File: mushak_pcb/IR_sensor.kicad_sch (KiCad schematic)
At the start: 24 parts, among them J6 IR_1, J7 IR_1, J8 IR_1, J9 IR_1, Q2 DMN3065LW-7, Q3 DMN3065LW-7, Q4 DMN3065LW-7, Q5 DMN3065LW-7

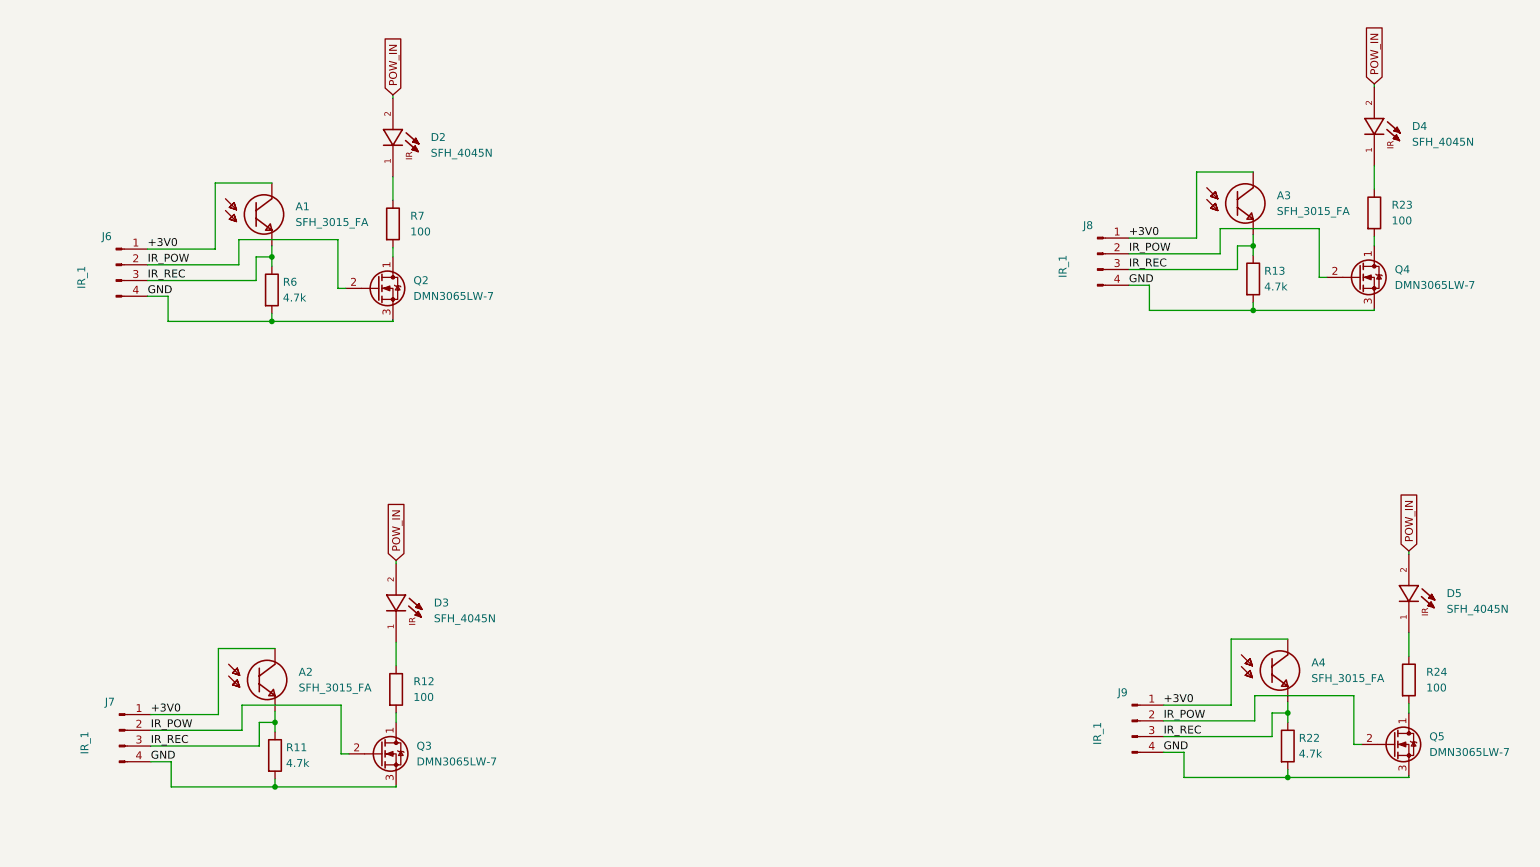
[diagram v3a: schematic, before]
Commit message: made draft pcb footprint placement
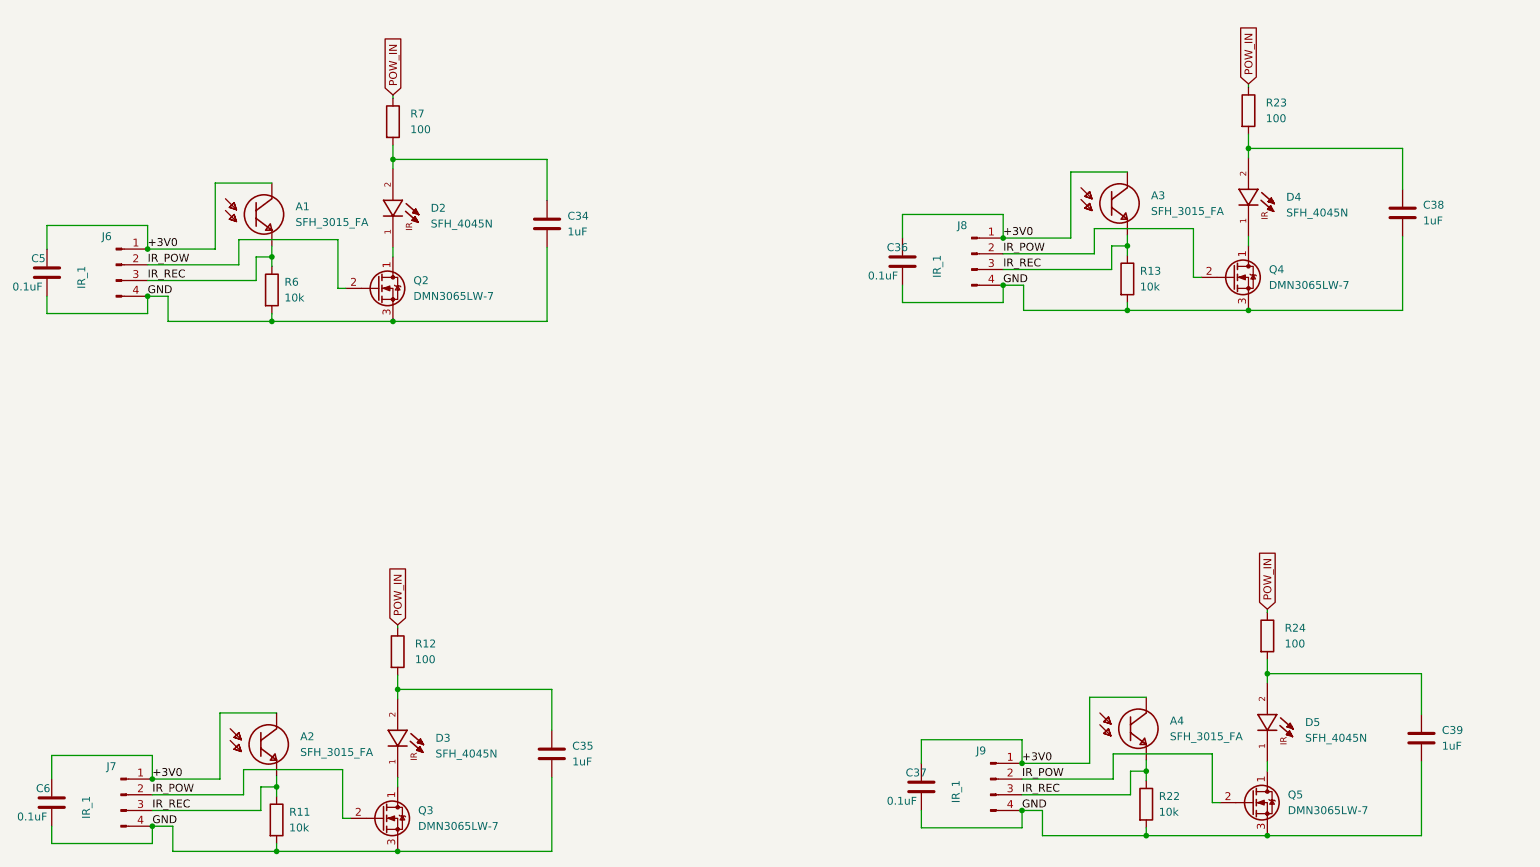
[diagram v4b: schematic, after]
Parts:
- added C34, C35, C38, C39: 1uF, Capacitor_SMD:C_0402_1005Metric, symbol Device:C
- added C36, C37, C5, C6: 0.1uF, Capacitor_SMD:C_0201_0603Metric, symbol Device:C
- R11, R13, R22, R6: value 4.7k -> 10k
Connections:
- net +3V0: now also C36.1, C37.1, C5.1, C6.1
- net GND: now also C34.2, C35.2, C36.2, C37.2, C38.2, C39.2, C5.2, C6.2
- net POW_IN: now also R12.1, R23.1, R24.1, R7.1; no longer D2.2, D3.2, D4.2, D5.2
- net at D2.1: now also Q2.1 (D); no longer R7.1
- net at D4.1: now also Q4.1 (D); no longer R23.1
- net at R23.2: now also D4.2, C38.1; no longer Q4.1 (D)
- net at D5.1: now also Q5.1 (D); no longer R24.1
- net at Q3.1 (D): now also D3.1; no longer R12.2
- net at R24.2: now also D5.2, C39.1; no longer Q5.1 (D)
- net at R7.2: now also D2.2, C34.1; no longer Q2.1 (D)
- new net: C35.1, D3.2, R12.2
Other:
- moved on the sheet: D2, R7

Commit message: corrected encoder and motor driver schematics
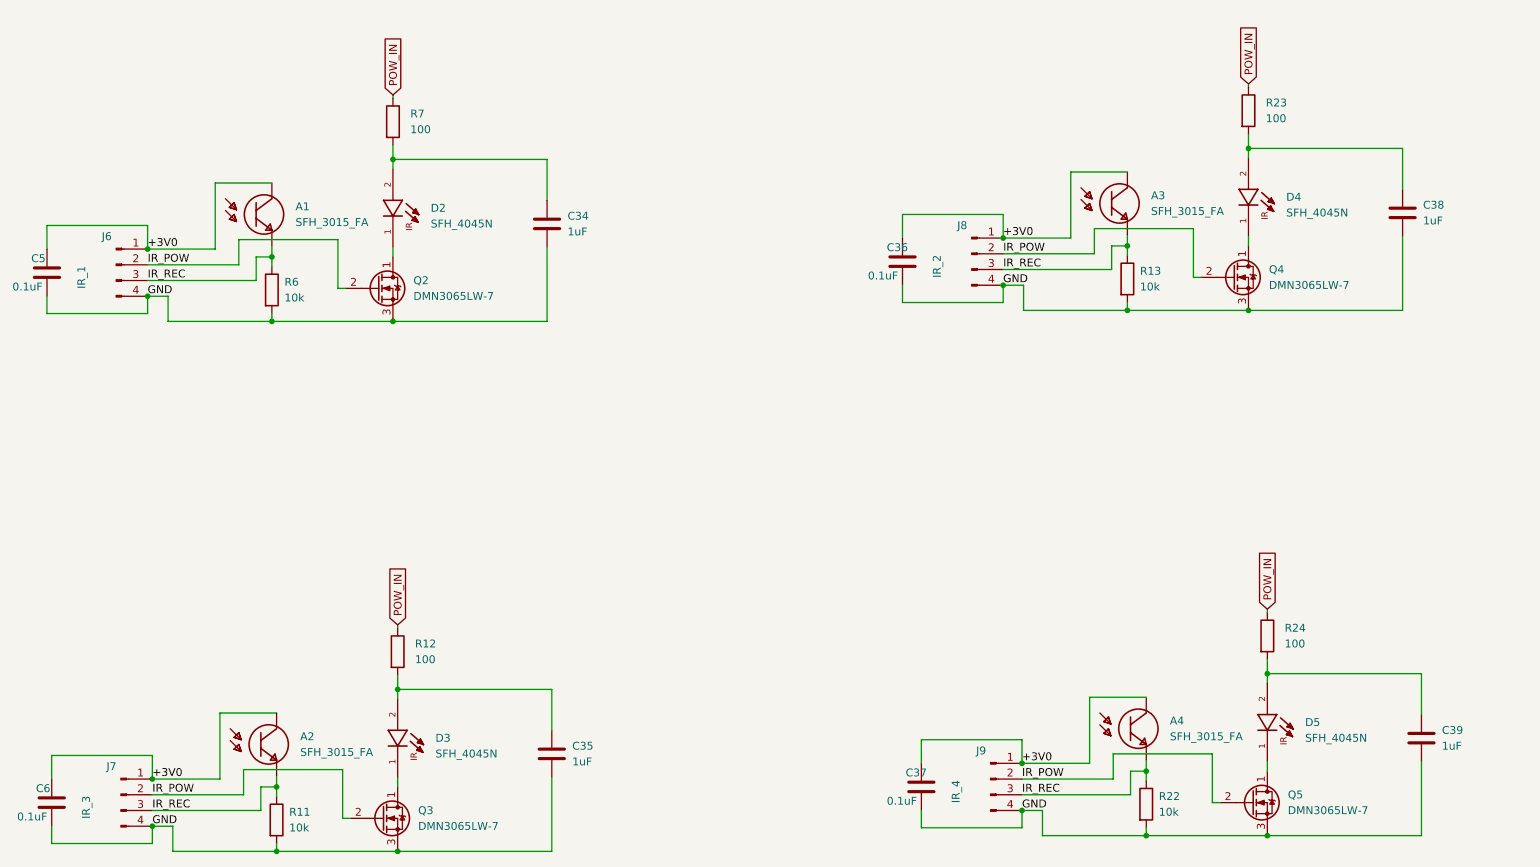
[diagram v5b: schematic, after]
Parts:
- J7: value IR_1 -> IR_3
- J8: value IR_1 -> IR_2
- J9: value IR_1 -> IR_4
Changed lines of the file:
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@@
     (in_bom yes) (on_board yes)
     (property "Reference" "J8" (id 0) (at 175.514 58.674 0))
-    (property "Value" "IR_1" (id 1) (at 171.45 65.278 90))
+    (property "Value" "IR_2" (id 1) (at 171.45 65.278 90))
     (property "Footprint" "mushak_mount_footprint:IR_SLAVE_V_04" (id 2) (at 177.038 63.246 0)
       (effects (font (size 1.27 1.27)) hide)
@@
     (in_bom yes) (on_board yes)
     (property "Reference" "J7" (id 0) (at 38.1 146.05 0))
-    (property "Value" "IR_1" (id 1) (at 34.036 152.654 90))
+    (property "Value" "IR_3" (id 1) (at 34.036 152.654 90))
     (property "Footprint" "mushak_mount_footprint:IR_SLAVE_V_04" (id 2) (at 39.624 150.622 0)
       (effects (font (size 1.27 1.27)) hide)
@@
     (in_bom yes) (on_board yes)
     (property "Reference" "J9" (id 0) (at 178.562 143.51 0))
-    (property "Value" "IR_1" (id 1) (at 174.498 150.114 90))
+    (property "Value" "IR_4" (id 1) (at 174.498 150.114 90))
     (property "Footprint" "mushak_mount_footprint:IR_SLAVE_V_04" (id 2) (at 180.086 148.082 0)
       (effects (font (size 1.27 1.27)) hide)

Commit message: changed footprint of passive components
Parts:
- C34, C35, C38, C39: footprint Capacitor_SMD:C_0402_1005Metric -> Capacitor_SMD:C_0603_1608Metric
- C36, C37, C5, C6: footprint Capacitor_SMD:C_0201_0603Metric -> Capacitor_SMD:C_0402_1005Metric
- R11, R13, R22, R6: footprint Resistor_SMD:R_0201_0603Metric -> Resistor_SMD:R_0402_1005Metric
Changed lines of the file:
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@@
       (effects (font (size 1.27 1.27)) (justify left))
     )
-    (property "Footprint" "Resistor_SMD:R_0201_0603Metric" (id 2) (at 62.992 154.686 90)
+    (property "Footprint" "Resistor_SMD:R_0402_1005Metric" (id 2) (at 62.992 154.686 90)
       (effects (font (size 1.27 1.27)) hide)
     )
@@
       (effects (font (size 1.27 1.27)) (justify left))
     )
-    (property "Footprint" "Capacitor_SMD:C_0201_0603Metric" (id 2) (at 29.4132 155.702 0)
+    (property "Footprint" "Capacitor_SMD:C_0402_1005Metric" (id 2) (at 29.4132 155.702 0)
       (effects (font (size 1.27 1.27)) hide)
     )
@@
       (effects (font (size 1.27 1.27)) (justify left))
     )
-    (property "Footprint" "Capacitor_SMD:C_0402_1005Metric" (id 2) (at 109.4232 62.23 0)
+    (property "Footprint" "Capacitor_SMD:C_0603_1608Metric" (id 2) (at 109.4232 62.23 0)
       (effects (font (size 1.27 1.27)) hide)
     )
@@
       (effects (font (size 1.27 1.27)) (justify left))
     )
-    (property "Footprint" "Capacitor_SMD:C_0402_1005Metric" (id 2) (at 110.1852 147.828 0)
+    (property "Footprint" "Capacitor_SMD:C_0603_1608Metric" (id 2) (at 110.1852 147.828 0)
       (effects (font (size 1.27 1.27)) hide)
     )
@@
       (effects (font (size 1.27 1.27)) (justify left))
     )
-    (property "Footprint" "Capacitor_SMD:C_0201_0603Metric" (id 2) (at 166.8272 68.326 0)
+    (property "Footprint" "Capacitor_SMD:C_0402_1005Metric" (id 2) (at 166.8272 68.326 0)
       (effects (font (size 1.27 1.27)) hide)
     )
@@
       (effects (font (size 1.27 1.27)) (justify left))
     )
-    (property "Footprint" "Capacitor_SMD:C_0201_0603Metric" (id 2) (at 28.6512 70.104 0)
+    (property "Footprint" "Capacitor_SMD:C_0402_1005Metric" (id 2) (at 28.6512 70.104 0)
       (effects (font (size 1.27 1.27)) hide)
     )
@@
       (effects (font (size 1.27 1.27)) (justify left))
     )
-    (property "Footprint" "Resistor_SMD:R_0201_0603Metric" (id 2) (at 62.23 69.088 90)
+    (property "Footprint" "Resistor_SMD:R_0402_1005Metric" (id 2) (at 62.23 69.088 90)
       (effects (font (size 1.27 1.27)) hide)
     )
@@
       (effects (font (size 1.27 1.27)) (justify left))
     )
-    (property "Footprint" "Capacitor_SMD:C_0402_1005Metric" (id 2) (at 247.5992 60.452 0)
+    (property "Footprint" "Capacitor_SMD:C_0603_1608Metric" (id 2) (at 247.5992 60.452 0)
       (effects (font (size 1.27 1.27)) hide)
     )
@@
       (effects (font (size 1.27 1.27)) (justify left))
     )
-    (property "Footprint" "Resistor_SMD:R_0201_0603Metric" (id 2) (at 200.406 67.31 90)
+    (property "Footprint" "Resistor_SMD:R_0402_1005Metric" (id 2) (at 200.406 67.31 90)
       (effects (font (size 1.27 1.27)) hide)
     )
@@
       (effects (font (size 1.27 1.27)) (justify left))
     )
-    (property "Footprint" "Resistor_SMD:R_0201_0603Metric" (id 2) (at 203.454 152.146 90)
+    (property "Footprint" "Resistor_SMD:R_0402_1005Metric" (id 2) (at 203.454 152.146 90)
       (effects (font (size 1.27 1.27)) hide)
     )
@@
       (effects (font (size 1.27 1.27)) (justify left))
     )
-    (property "Footprint" "Capacitor_SMD:C_0402_1005Metric" (id 2) (at 250.6472 145.288 0)
+    (property "Footprint" "Capacitor_SMD:C_0603_1608Metric" (id 2) (at 250.6472 145.288 0)
       (effects (font (size 1.27 1.27)) hide)
     )
@@
       (effects (font (size 1.27 1.27)) (justify left))
     )
-    (property "Footprint" "Capacitor_SMD:C_0201_0603Metric" (id 2) (at 169.8752 153.162 0)
-      (effects (font (size 1.27 1.27)) hide)
-    )
+    (property "Footprint" "Capacitor_SMD:C_0402_1005Metric" (id 2) (at 169.8752 153.162 0)
+      (effects (font (size 1.27 1.27)) hide)
+    )
